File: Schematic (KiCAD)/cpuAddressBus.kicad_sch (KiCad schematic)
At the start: 145 parts, among them J1 INVERT, J10 INVERT, J11 NAND_4, J12 INVERT, J13 NAND_4, J16 INVERT, J17 NAND_4, J18 INVERT, J19 NAND_4, J20 INVERT, J21 NAND_4, J22 INVERT, J23 NAND_4, J24 INVERT, J25 NAND_4, J26 INVERT, J27 NAND_4, J28 INVERT, J29 NAND_4, J30 INVERT, J31 NAND_4, J32 INVERT, J33 NAND_4, J34 INVERT, J35 NAND_4, J36 INVERT, J37 NAND_4, J38 INVERT, J39 NAND_4, J40 INVERT, J41 NAND_4, J42 INVERT, J43 NAND_2, J44 INVERT, J45 NAND_4, J46 INVERT, J47 NAND_4, J48 INVERT, J49 NAND_4, J50 INVERT, J51 NAND_3, J52 INVERT, J53 NAND_3, J54 INVERT, J55 NAND_3, J59 INVERT, J9 NAND_4, K1 INVERT, K18 INVERT, K2 INVERT, K25 INVERT, K27 INVERT, K3 INVERT, K30 INVERT, K34 INVERT, K36 INVERT, K37 INVERT, K39 INVERT, K4 INVERT, K44 INVERT, K47 INVERT, K48 INVERT, K5 NAND_3, K51 INVERT, K53 INVERT, K55 INVERT, K57 INVERT, K59 INVERT, K6 NAND_4, K63 INVERT, K68 INVERT, K70 INVERT, K74 INVERT, K82 INVERT, K84 INVERT, K88 INVERT, K89 INVERT, K90 INVERT, K98 INVERT, M2_Pinbuf_1 BUFFER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

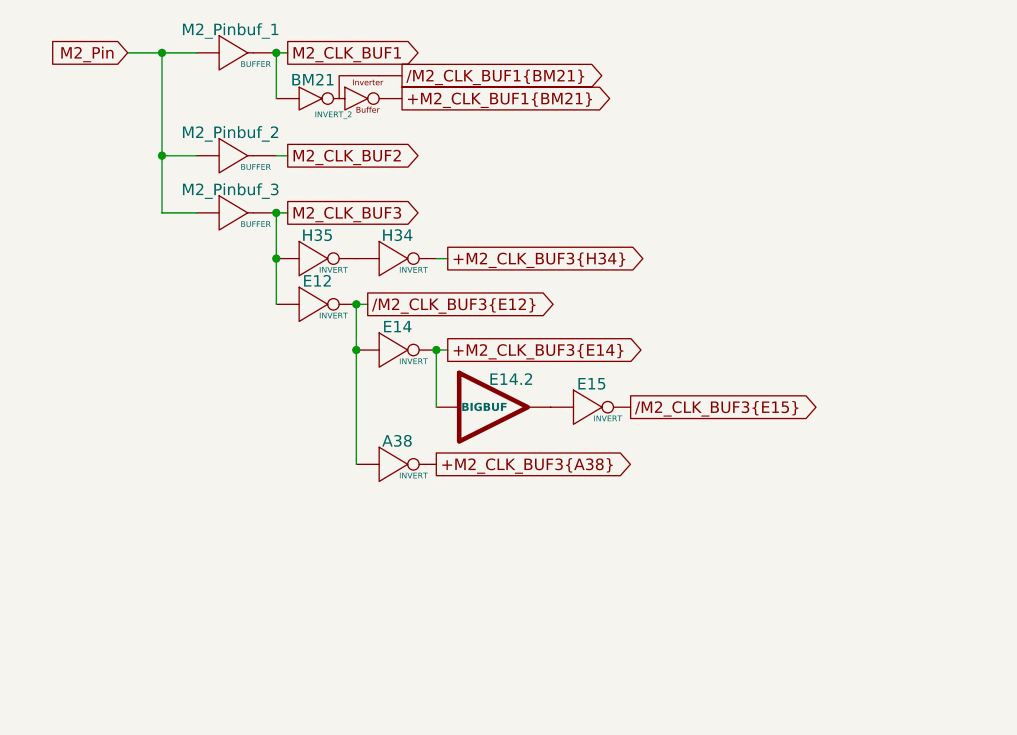
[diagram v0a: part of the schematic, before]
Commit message: - Started work on the pulse channels.  - Solved at least 2 of the red traces in the SVG.  - Finally realized that "Unknown 4to1" cells are actually just ordinary And-Or-Invert "AOI22" cells.
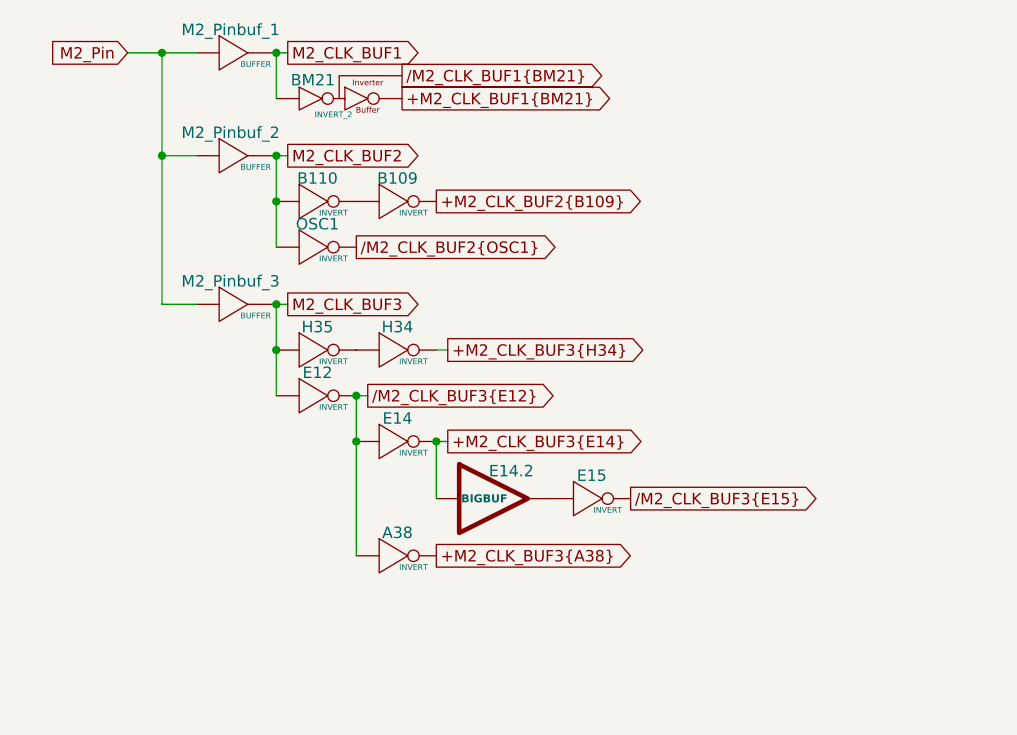
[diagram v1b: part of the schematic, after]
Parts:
- added B109, B110, OSC1: INVERT, symbol MMC5:INVERT
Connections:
- net M2_CLK_BUF2: now also B110. (X), OSC1. (X)
- net at H1. (X): now also K5. (X), K6. (X)
- new net: H2. (X), K18. (X), K30. (X), K36. (X), K48. (X), K63. (X), K74. (X), K89. (X), K98. (X)
- new net: H34. (X), H35. (X)
- new net: J1. (X), K6. (X)
- new net: H33. (X), H36. (X)
- new net: B109. (X), B110. (X)
- new net: E14.2. (X), E15. (X)
- new net +M2_CLK_BUF2{B109}: B109. (X)
- new net /M2_CLK_BUF2{OSC1}: OSC1. (X)
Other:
- moved on the sheet: A38, E12, E14, E14.2, E15, H34, H35, M2_Pinbuf_3

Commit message: - Pulse DAC logic is now complete.  - The 4-bit adders are verified correct using Excel.    - This revealed 1 tracing error and also 3 XNOR gates that are actually XOR in this case.  - Now including a PDF version of the schematic.
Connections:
- net at H1. (X): now also K5. (X), K6. (X)
- new net: H2. (X), K18. (X), K30. (X), K36. (X), K48. (X), K63. (X), K74. (X), K89. (X), K98. (X)
- new net: H34. (X), H35. (X)
- new net: J1. (X), K6. (X)
- new net: H33. (X), H36. (X)
- new net: B109. (X), B110. (X)
- new net: E14.2. (X), E15. (X)

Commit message: - All cells in the left and center areas have now been added into the schematics.  - Changed naming of the PDF files; I was accidentally writing over furrtek's original with my new PDF.
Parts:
- added E25: BUFFER, symbol MMC5:BUFFER
- added E27, J56, J57, J58, K23, K62, L19, L20: INVERT, symbol MMC5:INVERT
- added J14, K24: NAND_2, symbol MMC5:NAND_2
- added J15, K61, L60: NAND_3, symbol MMC5:NAND_3
- added J3: BIGBUF, symbol MMC5:BIGBUF
- added L61: NOR_3, symbol MMC5:NOR_3
- renumbered E24 to E23,E24
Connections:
- net +M2_CLK_BUF3{E14}: now also E25. (X)
- net +M2_CLK_BUF3{H34}: now also J3. (X)
- net CPU_R/W_Pin: now also E27. (X)
- net at H1. (X): now also K5. (X), K6. (X)
- net /ROMSEL{E23,E24}: now reaches E23,E24. (X)
- new net: L60. (X), L61. (X)
- new net: J15. (X), L61. (X)
- new net: H2. (X), K18. (X), K30. (X), K36. (X), K48. (X), K63. (X), K74. (X), K89. (X), K98. (X)
- new net: H34. (X), H35. (X)
- new net: K23. (X), L20. (X)
- new net: J58. (X), L20. (X)
- new net: J56. (X), J57. (X)
- new net: J56. (X), K62. (X)
- new net: J1. (X), K6. (X)
- new net: H33. (X), H36. (X)
- new net: K61. (X), L60. (X)
- new net: J3. (X), L19. (X)
- new net: J15. (X), L19. (X)
- new net: J57. (X), J58. (X)
- new net: K61. (X), K62. (X)
- new net: J14. (X), K24. (X) (x2)
- new net: B109. (X), B110. (X)
- new net: K23. (X), K24. (X)
- new net: E14.2. (X), E15. (X)
- new net +M2_CLK_BUF3{E25}: E25. (X)
- new net /CPU_R/W{E27}: E27. (X)
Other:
- note added: "M2 Spaghetti That Goes Nowhere"
- moved on the sheet: A38, E12, E14, E14.2, E15, E23,E24

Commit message: - All known gates and traces are now accounted for in the schematics!  :)
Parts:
- removed J14, K24: NAND_2, symbol MMC5:NAND_2
- removed J15, K61, L60: NAND_3, symbol MMC5:NAND_3
- removed J3: BIGBUF, symbol MMC5:BIGBUF
- removed J56, J57, J58, K23, K62, L19, L20: INVERT, symbol MMC5:INVERT
- removed L61: NOR_3, symbol MMC5:NOR_3
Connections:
- net at H1. (X): now also K5. (X), K6. (X)
- new net: H2. (X), K18. (X), K30. (X), K36. (X), K48. (X), K63. (X), K74. (X), K89. (X), K98. (X)
- new net: H34. (X), H35. (X)
- new net: J1. (X), K6. (X)
- new net: H33. (X), H36. (X)
- new net: B109. (X), B110. (X)
- new net: E14.2. (X), E15. (X)
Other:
- note added: "/ROMSEL, Register Access"
- note added: "CPU R/W, Register Read/Write"
- note added: "M2 Clock Buffering"
- note removed: "M2 Spaghetti That Goes Nowhere"
- moved on the sheet: A38, B109, B110, BK88, BM21, E12, E14, E14.2, E15, E23,E24, E25, E27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
